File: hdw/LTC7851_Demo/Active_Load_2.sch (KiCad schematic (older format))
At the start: 0 parts

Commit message: Added active load sheets
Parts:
- added J? (x2): ISNS, symbol Connector_Generic:Conn_01x02
- added Q? (x2): BSC123N10LSGATMA1, Package_TO_SOT_SMD:TDSON-8-1, symbol Transistor_FET:BSC123N10LSG
- added R? (x2): 5m, symbol Custom_Library:R_Custom
- added R? (x2): 10k, symbol Custom_Library:R_Custom
- added R? (x2): 10, symbol Custom_Library:R_Custom
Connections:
- net labels added: +5V, GND, LOAD_GATE
- wire segments 0 -> 12

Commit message: Annotated schematic
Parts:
- gave numbers to parts that had none: 10
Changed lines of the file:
@@
 $EndDescr
 $Comp
-L Transistor_FET:BSC123N10LSG Q?
+L Transistor_FET:BSC123N10LSG Q1201
 U 1 1 5BC43333
 P 7900 2420
-F 0 "Q?" H 8100 2495 50  0000 L CNN
+F 0 "Q1201" H 8100 2495 50  0000 L CNN
 F 1 "BSC123N10LSGATMA1" H 8100 2420 50  0000 L CNN
 F 2 "Package_TO_SOT_SMD:TDSON-8-1" H 8100 2345 50  0001 L CIN
@@
 	8000 2790 8000 2700
 $Comp
-L power:GND #PWR?
+L power:GND #PWR01204
 U 1 1 5BC4333B
 P 8000 3090
-F 0 "#PWR?" H 8000 2840 50  0001 C CNN
+F 0 "#PWR01204" H 8000 2840 50  0001 C CNN
 F 1 "GND" H 8000 2940 50  0000 C CNN
 F 2 "" H 8000 3090 50  0001 C CNN
@@
 $EndComp
 $Comp
-L Connector_Generic:Conn_01x02 J?
+L Connector_Generic:Conn_01x02 J1201
 U 1 1 5BC43341
 P 8830 2700
-F 0 "J?" H 8830 2800 50  0000 C CNN
+F 0 "J1201" H 8830 2800 50  0000 C CNN
 F 1 "ISNS" H 8830 2500 50  0000 C CNN
 F 2 "" H 8830 2700 50  0001 C CNN
@@
 	8000 2700 8000 2620
 $Comp
-L power:GND #PWR?
+L power:GND #PWR01207
 U 1 1 5BC4334B
 P 8630 2800
-F 0 "#PWR?" H 8630 2550 50  0001 C CNN
+F 0 "#PWR01207" H 8630 2550 50  0001 C CNN
 F 1 "GND" H 8630 2650 50  0000 C CNN
 F 2 "" H 8630 2800 50  0001 C CNN
@@
 AR Path="/5BB86F29/5BC43355" Ref="R?"  Part="1"
 AR Path="/5BBF20D5/5BC43355" Ref="R?"  Part="1"
-AR Path="/5BBF20D8/5BC43355" Ref="R?"  Part="1"
-F 0 "R?" H 7900 2940 50  0000 R CNN
+AR Path="/5BBF20D8/5BC43355" Ref="R1205"  Part="1"
+F 0 "R1205" H 7900 2940 50  0000 R CNN
 F 1 "5m" V 8000 2940 50  0000 C CNN
 F 2 "" H 8000 2940 50  0001 C CNN
@@
 $EndComp
 $Comp
-L power:+5V #PWR?
+L power:+5V #PWR01203
 U 1 1 5BC4335C
 P 8000 2220
-F 0 "#PWR?" H 8000 2070 50  0001 C CNN
+F 0 "#PWR01203" H 8000 2070 50  0001 C CNN
 F 1 "+5V" H 8000 2360 50  0000 C CNN
 F 2 "" H 8000 2220 50  0001 C CNN
@@
 AR Path="/5BB86F23/5BC43366" Ref="R?"  Part="1"
 AR Path="/5BBF20D5/5BC43366" Ref="R?"  Part="1"
-AR Path="/5BBF20D8/5BC43366" Ref="R?"  Part="1"
-F 0 "R?" H 7140 2640 50  0000 R CNN
+AR Path="/5BBF20D8/5BC43366" Ref="R1203"  Part="1"
+F 0 "R1203" H 7140 2640 50  0000 R CNN
 F 1 "10k" V 7240 2640 50  0000 C CNN
 F 2 "" H 7240 2640 50  0001 C CNN
@@
 $EndComp
 $Comp
-L power:GND #PWR?
+L power:GND #PWR01201
 U 1 1 5BC4336D
 P 7240 2790
-F 0 "#PWR?" H 7240 2540 50  0001 C CNN
+F 0 "#PWR01201" H 7240 2540 50  0001 C CNN
 F 1 "GND" H 7240 2640 50  0000 C CNN
 F 2 "" H 7240 2790 50  0001 C CNN
@@
 	7240 2420 7700 2420
 $Comp
-L Custom_Library:R_Custom R?
+L Custom_Library:R_Custom R1201
 U 1 1 5BC43379
 P 6560 2420
-F 0 "R?" V 6460 2420 50  0000 C CNN
+F 0 "R1201" V 6460 2420 50  0000 C CNN
 F 1 "10" V 6560 2420 50  0000 C CNN
 F 2 "" H 6560 2420 50  0001 C CNN
@@
 LOAD_GATE
 $Comp
-L Transistor_FET:BSC123N10LSG Q?
+L Transistor_FET:BSC123N10LSG Q1202
 U 1 1 5BC43384
 P 7900 4460
-F 0 "Q?" H 8100 4535 50  0000 L CNN
+F 0 "Q1202" H 8100 4535 50  0000 L CNN
 F 1 "BSC123N10LSGATMA1" H 8100 4460 50  0000 L CNN
 F 2 "Package_TO_SOT_SMD:TDSON-8-1" H 8100 4385 50  0001 L CIN
@@
 	8000 4830 8000 4740
 $Comp
-L power:GND #PWR?
+L power:GND #PWR01206
 U 1 1 5BC4338C
 P 8000 5130
-F 0 "#PWR?" H 8000 4880 50  0001 C CNN
+F 0 "#PWR01206" H 8000 4880 50  0001 C CNN
 F 1 "GND" H 8000 4980 50  0000 C CNN
 F 2 "" H 8000 5130 50  0001 C CNN
@@
 $EndComp
 $Comp
-L Connector_Generic:Conn_01x02 J?
+L Connector_Generic:Conn_01x02 J1202
 U 1 1 5BC43392
 P 8830 4740
-F 0 "J?" H 8830 4840 50  0000 C CNN
+F 0 "J1202" H 8830 4840 50  0000 C CNN
 F 1 "ISNS" H 8830 4540 50  0000 C CNN
 F 2 "" H 8830 4740 50  0001 C CNN
@@
 	8000 4740 8000 4660
 $Comp
-L power:GND #PWR?
+L power:GND #PWR01208
 U 1 1 5BC4339C
 P 8630 4840
-F 0 "#PWR?" H 8630 4590 50  0001 C CNN
+F 0 "#PWR01208" H 8630 4590 50  0001 C CNN
 F 1 "GND" H 8630 4690 50  0000 C CNN
 F 2 "" H 8630 4840 50  0001 C CNN
@@
 AR Path="/5BB86F29/5BC433A6" Ref="R?"  Part="1"
 AR Path="/5BBF20D5/5BC433A6" Ref="R?"  Part="1"
-AR Path="/5BBF20D8/5BC433A6" Ref="R?"  Part="1"
-F 0 "R?" H 7900 4980 50  0000 R CNN
+AR Path="/5BBF20D8/5BC433A6" Ref="R1206"  Part="1"
+F 0 "R1206" H 7900 4980 50  0000 R CNN
 F 1 "5m" V 8000 4980 50  0000 C CNN
 F 2 "" H 8000 4980 50  0001 C CNN
@@
 $EndComp
 $Comp
-L power:+5V #PWR?
+L power:+5V #PWR01205
 U 1 1 5BC433AD
 P 8000 4260
-F 0 "#PWR?" H 8000 4110 50  0001 C CNN
+F 0 "#PWR01205" H 8000 4110 50  0001 C CNN
 F 1 "+5V" H 8000 4400 50  0000 C CNN
 F 2 "" H 8000 4260 50  0001 C CNN
@@
 AR Path="/5BB86F23/5BC433B7" Ref="R?"  Part="1"
 AR Path="/5BBF20D5/5BC433B7" Ref="R?"  Part="1"
-AR Path="/5BBF20D8/5BC433B7" Ref="R?"  Part="1"
-F 0 "R?" H 7140 4680 50  0000 R CNN
+AR Path="/5BBF20D8/5BC433B7" Ref="R1204"  Part="1"
+F 0 "R1204" H 7140 4680 50  0000 R CNN
 F 1 "10k" V 7240 4680 50  0000 C CNN
 F 2 "" H 7240 4680 50  0001 C CNN
@@
 $EndComp
 $Comp
-L power:GND #PWR?
+L power:GND #PWR01202
 U 1 1 5BC433BE
 P 7240 4830
-F 0 "#PWR?" H 7240 4580 50  0001 C CNN
+F 0 "#PWR01202" H 7240 4580 50  0001 C CNN
 F 1 "GND" H 7240 4680 50  0000 C CNN
 F 2 "" H 7240 4830 50  0001 C CNN
@@
 	7240 4460 7700 4460
 $Comp
-L Custom_Library:R_Custom R?
+L Custom_Library:R_Custom R1202
 U 1 1 5BC433CA
 P 6560 4460
-F 0 "R?" V 6460 4460 50  0000 C CNN
+F 0 "R1202" V 6460 4460 50  0000 C CNN
 F 1 "10" V 6560 4460 50  0000 C CNN
 F 2 "" H 6560 4460 50  0001 C CNN

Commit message: Added Digi-Key part numbers for all parts
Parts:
- R1201, R1202: Digi-Key PN PN -> YAG3351CT-ND
- R1203, R1204: Digi-Key PN PN -> RHM10KADCT-ND
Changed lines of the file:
@@
 F 5 "1%" H 7320 2640 50  0000 L CNN "Tolerance"
 F 6 "1/10W" H 7320 2560 50  0000 L CNN "Wattage"
-F 7 "PN" H 7540 3040 60  0001 C CNN "Digi-Key PN"
+F 7 "RHM10KADCT-ND" H 7540 3040 60  0001 C CNN "Digi-Key PN"
 	1    7240 2640
 	1    0    0    -1
@@
 F 5 "1%" V 6760 2420 50  0000 C CNN "Tolerance"
 F 6 "1/10W" V 6860 2420 50  0000 C CNN "Wattage"
-F 7 "PN" H 6860 2820 60  0001 C CNN "Digi-Key PN"
+F 7 "YAG3351CT-ND" H 6860 2820 60  0001 C CNN "Digi-Key PN"
 	1    6560 2420
 	0    1    1    0
@@
 F 5 "1%" H 7320 4680 50  0000 L CNN "Tolerance"
 F 6 "1/10W" H 7320 4600 50  0000 L CNN "Wattage"
-F 7 "PN" H 7540 5080 60  0001 C CNN "Digi-Key PN"
+F 7 "RHM10KADCT-ND" H 7540 5080 60  0001 C CNN "Digi-Key PN"
 	1    7240 4680
 	1    0    0    -1
@@
 F 5 "1%" V 6760 4460 50  0000 C CNN "Tolerance"
 F 6 "1/10W" V 6860 4460 50  0000 C CNN "Wattage"
-F 7 "PN" H 6860 4860 60  0001 C CNN "Digi-Key PN"
+F 7 "YAG3351CT-ND" H 6860 4860 60  0001 C CNN "Digi-Key PN"
 	1    6560 4460
 	0    1    1    0

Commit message: Assigned footprints
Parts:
- J1201, J1202: footprint (none) -> Pin_Headers:Pin_Header_Straight_1x02_Pitch2.54mm
- Q1201, Q1202: footprint Package_TO_SOT_SMD:TDSON-8-1 -> TO_SOT_Packages_SMD:TDSON-8-1
- R1201, R1202, R1203, R1204: footprint (none) -> Resistors_SMD:R_0603
- R1205, R1206: footprint (none) -> Resistors_SMD:R_2512
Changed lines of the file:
@@
 F 0 "Q1201" H 8100 2495 50  0000 L CNN
 F 1 "BSC123N10LSGATMA1" H 8100 2420 50  0000 L CNN
-F 2 "Package_TO_SOT_SMD:TDSON-8-1" H 8100 2345 50  0001 L CIN
+F 2 "TO_SOT_Packages_SMD:TDSON-8-1" H 8100 2345 50  0001 L CIN
 F 3 "http://www.infineon.com/dgdl/Infineon-BSC123N10LS-DS-v02_08-en.pdf?fileId=db3a30431b3e89eb011b4626974b7df5" V 7900 2420 50  0001 L CNN
 F 4 "BSC123N10LSGATMA1CT-ND" H 7900 2420 50  0001 C CNN "Digi-Key PN"
@@
 F 0 "J1201" H 8830 2800 50  0000 C CNN
 F 1 "ISNS" H 8830 2500 50  0000 C CNN
-F 2 "" H 8830 2700 50  0001 C CNN
+F 2 "Pin_Headers:Pin_Header_Straight_1x02_Pitch2.54mm" H 8830 2700 50  0001 C CNN
 F 3 "~" H 8830 2700 50  0001 C CNN
 	1    8830 2700
@@
 F 0 "R1205" H 7900 2940 50  0000 R CNN
 F 1 "5m" V 8000 2940 50  0000 C CNN
-F 2 "" H 8000 2940 50  0001 C CNN
+F 2 "Resistors_SMD:R_2512" H 8000 2940 50  0001 C CNN
 F 3 "" H 8000 2940 50  0001 C CNN
 F 4 "YAG2145CT-ND" H 8300 3340 60  0001 C CNN "Digi-Key PN"
@@
 F 0 "R1203" H 7140 2640 50  0000 R CNN
 F 1 "10k" V 7240 2640 50  0000 C CNN
-F 2 "" H 7240 2640 50  0001 C CNN
+F 2 "Resistors_SMD:R_0603" H 7240 2640 50  0001 C CNN
 F 3 "" H 7240 2640 50  0001 C CNN
 F 4 "0603" H 7320 2720 50  0000 L CNN "display_footprint"
@@
 F 0 "R1201" V 6460 2420 50  0000 C CNN
 F 1 "10" V 6560 2420 50  0000 C CNN
-F 2 "" H 6560 2420 50  0001 C CNN
+F 2 "Resistors_SMD:R_0603" H 6560 2420 50  0001 C CNN
 F 3 "" H 6560 2420 50  0001 C CNN
 F 4 "0603" V 6660 2420 50  0000 C CNN "display_footprint"
@@
 F 0 "Q1202" H 8100 4535 50  0000 L CNN
 F 1 "BSC123N10LSGATMA1" H 8100 4460 50  0000 L CNN
-F 2 "Package_TO_SOT_SMD:TDSON-8-1" H 8100 4385 50  0001 L CIN
+F 2 "TO_SOT_Packages_SMD:TDSON-8-1" H 8100 4385 50  0001 L CIN
 F 3 "http://www.infineon.com/dgdl/Infineon-BSC123N10LS-DS-v02_08-en.pdf?fileId=db3a30431b3e89eb011b4626974b7df5" V 7900 4460 50  0001 L CNN
 F 4 "BSC123N10LSGATMA1CT-ND" H 7900 4460 50  0001 C CNN "Digi-Key PN"
@@
 F 0 "J1202" H 8830 4840 50  0000 C CNN
 F 1 "ISNS" H 8830 4540 50  0000 C CNN
-F 2 "" H 8830 4740 50  0001 C CNN
+F 2 "Pin_Headers:Pin_Header_Straight_1x02_Pitch2.54mm" H 8830 4740 50  0001 C CNN
 F 3 "~" H 8830 4740 50  0001 C CNN
 	1    8830 4740
@@
 F 0 "R1206" H 7900 4980 50  0000 R CNN
 F 1 "5m" V 8000 4980 50  0000 C CNN
-F 2 "" H 8000 4980 50  0001 C CNN
+F 2 "Resistors_SMD:R_2512" H 8000 4980 50  0001 C CNN
 F 3 "" H 8000 4980 50  0001 C CNN
 F 4 "YAG2145CT-ND" H 8300 5380 60  0001 C CNN "Digi-Key PN"
@@
 F 0 "R1204" H 7140 4680 50  0000 R CNN
 F 1 "10k" V 7240 4680 50  0000 C CNN
-F 2 "" H 7240 4680 50  0001 C CNN
+F 2 "Resistors_SMD:R_0603" H 7240 4680 50  0001 C CNN
 F 3 "" H 7240 4680 50  0001 C CNN
 F 4 "0603" H 7320 4760 50  0000 L CNN "display_footprint"
@@
 F 0 "R1202" V 6460 4460 50  0000 C CNN
 F 1 "10" V 6560 4460 50  0000 C CNN
-F 2 "" H 6560 4460 50  0001 C CNN
+F 2 "Resistors_SMD:R_0603" H 6560 4460 50  0001 C CNN
 F 3 "" H 6560 4460 50  0001 C CNN
 F 4 "0603" V 6660 4460 50  0000 C CNN "display_footprint"

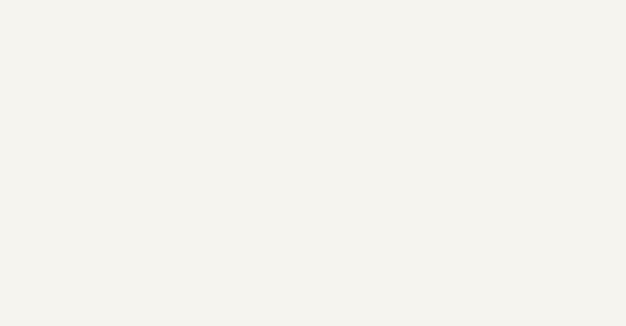
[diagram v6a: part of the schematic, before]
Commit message: Added page titles
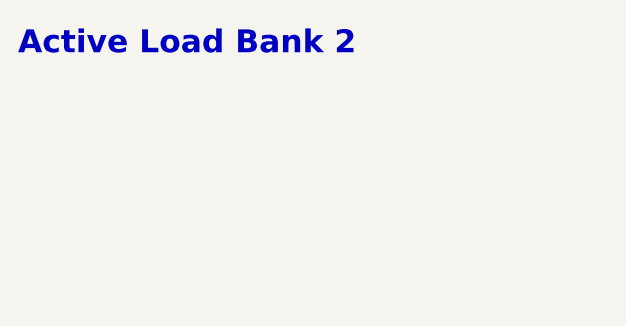
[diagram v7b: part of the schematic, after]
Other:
- note added: "Active Load Bank 2"
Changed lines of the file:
@@
 Text GLabel 6410 4460 0    50   Input ~ 0
 LOAD_GATE
+Text Notes 540  690  0    100  ~ 20
+Active Load Bank 2
 $EndSCHEMATC

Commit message: Placed phases on board
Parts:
- removed J1201, J1202: ISNS, Pin_Headers:Pin_Header_Straight_1x02_Pitch2.54mm, symbol Connector_Generic:Conn_01x02
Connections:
- wire segments 12 -> 8
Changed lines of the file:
@@
 	1    0    0    -1
 $EndComp
-Wire Wire Line
-	8000 2790 8000 2700
 $Comp
 L power:GND #PWR01204
@@
 F 3 "" H 8000 3090 50  0001 C CNN
 	1    8000 3090
-	1    0    0    -1
-$EndComp
-$Comp
-L Connector_Generic:Conn_01x02 J1201
-U 1 1 5BC43341
-P 8830 2700
-F 0 "J1201" H 8830 2800 50  0000 C CNN
-F 1 "ISNS" H 8830 2500 50  0000 C CNN
-F 2 "Pin_Headers:Pin_Header_Straight_1x02_Pitch2.54mm" H 8830 2700 50  0001 C CNN
-F 3 "~" H 8830 2700 50  0001 C CNN
-	1    8830 2700
-	1    0    0    -1
-$EndComp
-Wire Wire Line
-	8630 2700 8000 2700
-Connection ~ 8000 2700
-Wire Wire Line
-	8000 2700 8000 2620
-$Comp
-L power:GND #PWR01207
-U 1 1 5BC4334B
-P 8630 2800
-F 0 "#PWR01207" H 8630 2550 50  0001 C CNN
-F 1 "GND" H 8630 2650 50  0000 C CNN
-F 2 "" H 8630 2800 50  0001 C CNN
-F 3 "" H 8630 2800 50  0001 C CNN
-	1    8630 2800
 	1    0    0    -1
 $EndComp
@@
 	1    0    0    -1
 $EndComp
-Wire Wire Line
-	8000 4830 8000 4740
 $Comp
 L power:GND #PWR01206
@@
 F 3 "" H 8000 5130 50  0001 C CNN
 	1    8000 5130
-	1    0    0    -1
-$EndComp
-$Comp
-L Connector_Generic:Conn_01x02 J1202
-U 1 1 5BC43392
-P 8830 4740
-F 0 "J1202" H 8830 4840 50  0000 C CNN
-F 1 "ISNS" H 8830 4540 50  0000 C CNN
-F 2 "Pin_Headers:Pin_Header_Straight_1x02_Pitch2.54mm" H 8830 4740 50  0001 C CNN
-F 3 "~" H 8830 4740 50  0001 C CNN
-	1    8830 4740
-	1    0    0    -1
-$EndComp
-Wire Wire Line
-	8630 4740 8000 4740
-Connection ~ 8000 4740
-Wire Wire Line
-	8000 4740 8000 4660
-$Comp
-L power:GND #PWR01208
-U 1 1 5BC4339C
-P 8630 4840
-F 0 "#PWR01208" H 8630 4590 50  0001 C CNN
-F 1 "GND" H 8630 4690 50  0000 C CNN
-F 2 "" H 8630 4840 50  0001 C CNN
-F 3 "" H 8630 4840 50  0001 C CNN
-	1    8630 4840
 	1    0    0    -1
 $EndComp
@@
 Text Notes 540  690  0    100  ~ 20
 Active Load Bank 2
+Wire Wire Line
+	8000 2620 8000 2790
+Wire Wire Line
+	8000 4660 8000 4830
 $EndSCHEMATC
